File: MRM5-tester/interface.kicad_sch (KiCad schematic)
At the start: 21 parts, among them J1 Conn_01x05, J2 Conn_01x02, J3 GSB1C41110SSHR, J5 Conn_01x02, J6 Conn_01x02, J7 Conn_01x02, U3 CP2102N-A02-GQFN20

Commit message: tester PCB 작성중
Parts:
- removed J5, J6: Conn_01x02, Connector_PinHeader_2.54mm:PinHeader_1x02_P2.54mm_Vertical, symbol PCM_4ms_Connector:Conn_01x02
- added P1, P2: ~, Mouser:PAD_Hole_D2mm, symbol Mouser:PAD_hole2.6
- renumbered C5 to C3, C6 to C4, C7 to C5, C8 to C6, D1 to D5, D2 to D6, D3 to D7, D4 to D8, J3 to J2, J7 to J3, J2 to J4, R3 to R10, R4 to R11, R5 to R12, R6 to R13, R7 to R14, R2 to R9, U3 to U1
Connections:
- new net Vn_h: P2.1
- new net Vp_h: P1.1
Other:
- moved on the sheet: C3, C4, C5, C6, D5, D6, D7, D8, J1, J2, J3, J4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

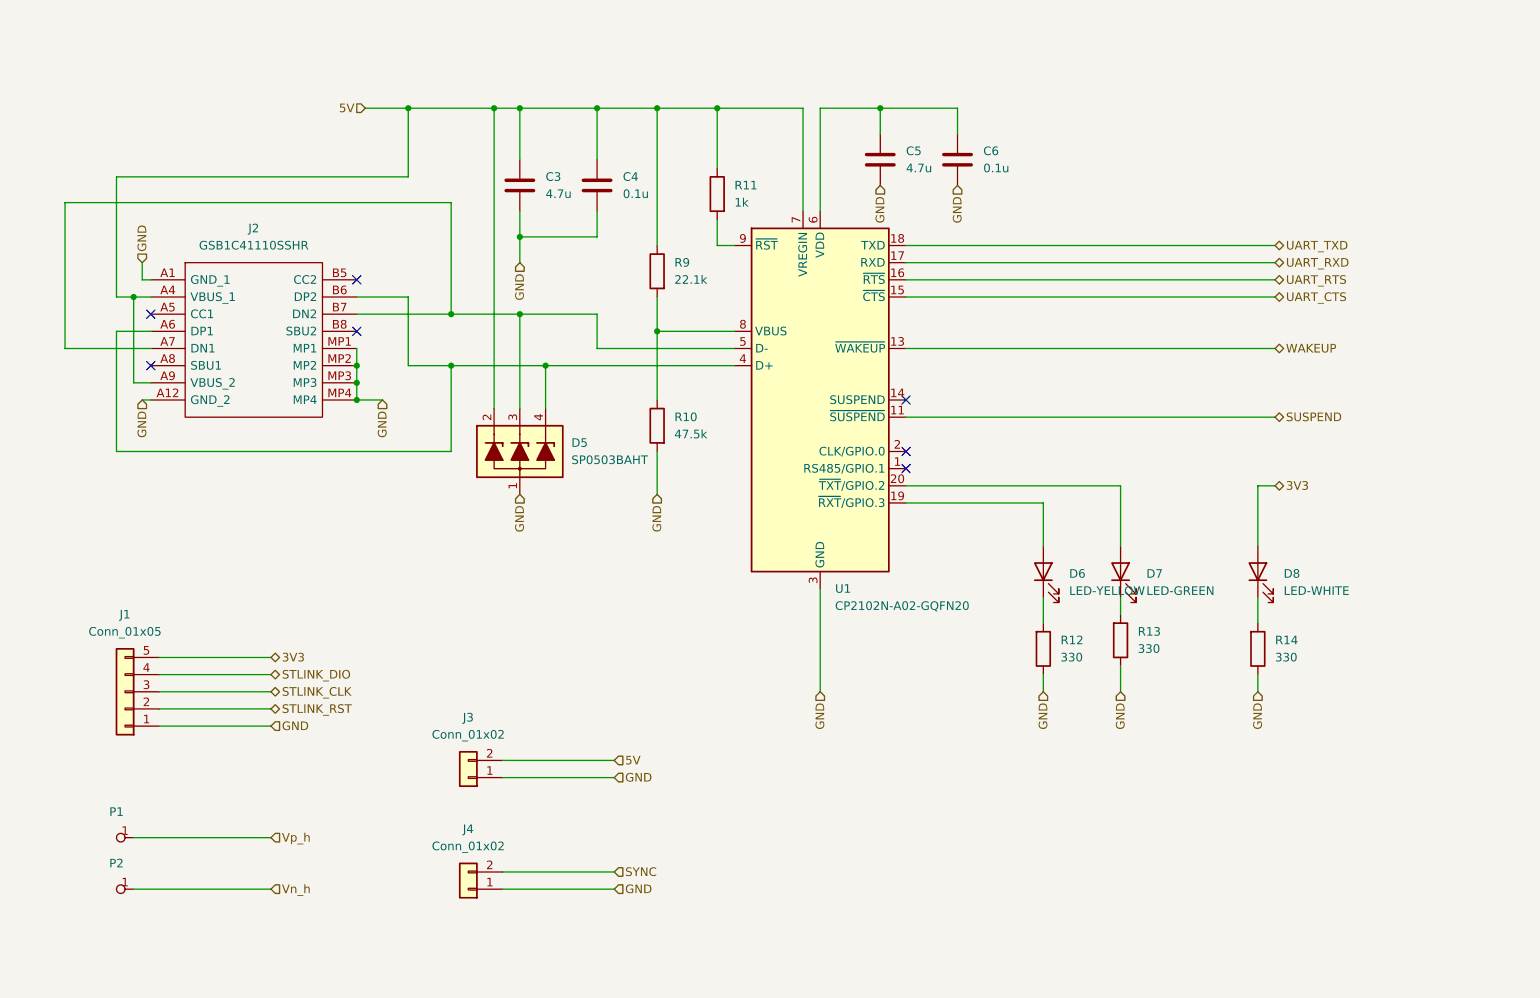
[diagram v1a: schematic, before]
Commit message: tester pcb 디자인 완료
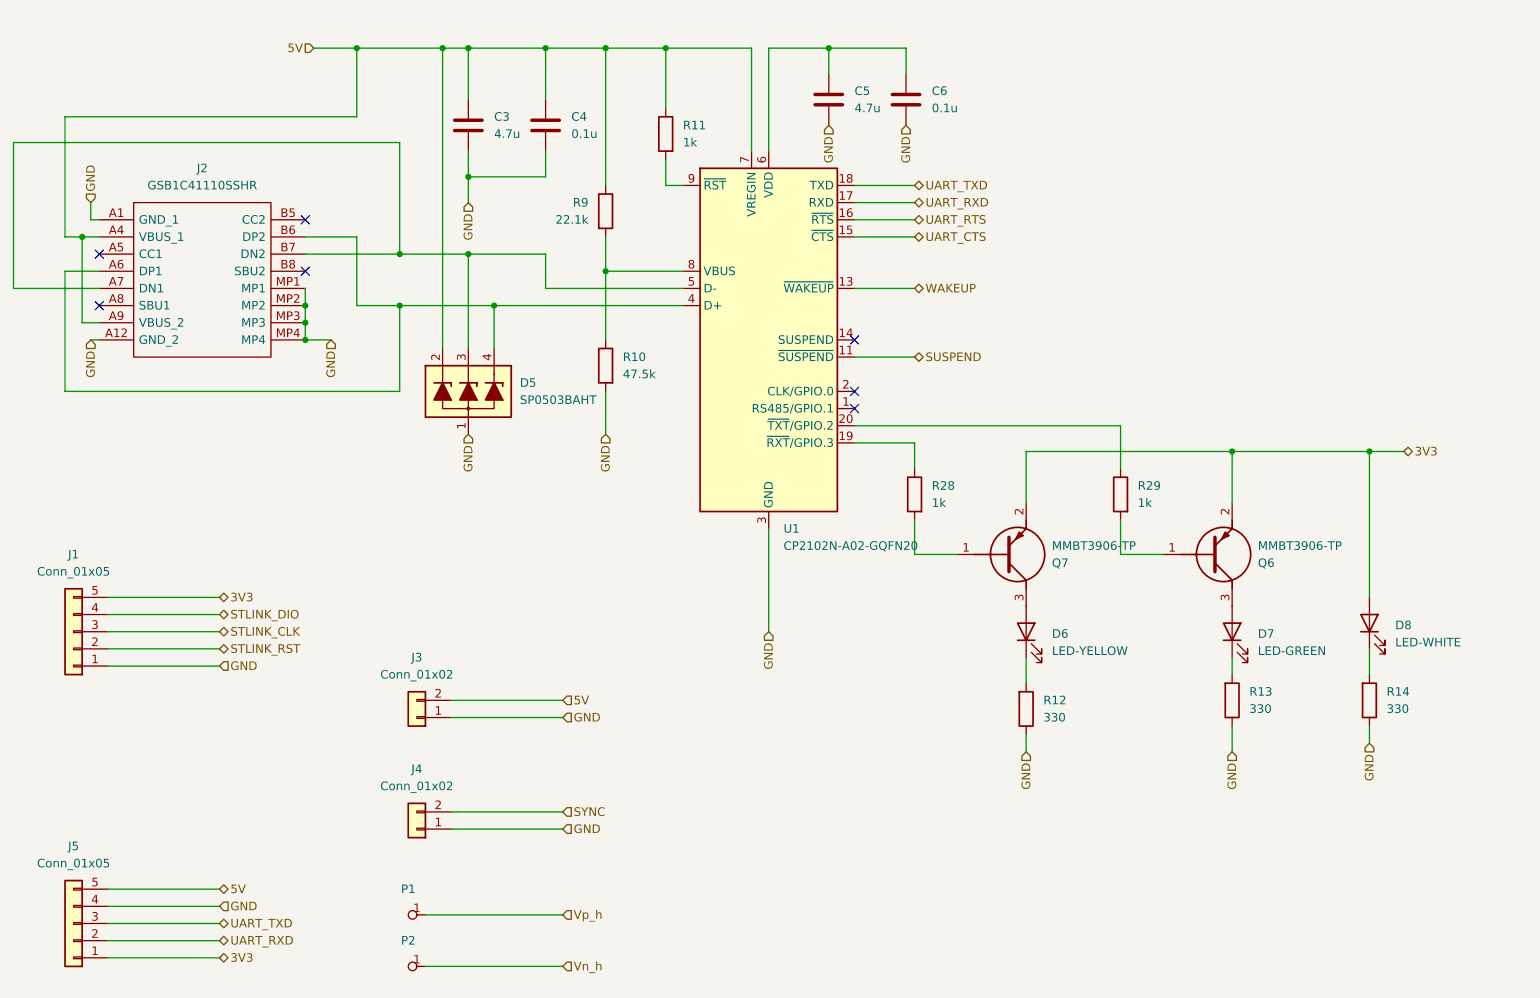
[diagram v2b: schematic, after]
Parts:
- added J5: Conn_01x05, Connector_PinSocket_2.54mm:PinSocket_1x05_P2.54mm_Vertical, symbol Connector_Generic:Conn_01x05
- added Q6, Q7: MMBT3906-TP, Mouser:SOT95P237X125-3N, symbol ktw07182:MMBT3906-TP
- added R28, R29: 1k, PCM_Resistor_SMD_AKL:R_0402_1005Metric, symbol PCM_Resistor_AKL:R_0402
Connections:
- net 3V3: now also J5.1 (Pin_1), Q6.2 (E), Q7.2 (E)
- net 5V: now also J5.5 (Pin_5)
- net GND: now also J5.4 (Pin_4)
- net UART_RXD: now also J5.2 (Pin_2)
- net UART_TXD: now also J5.3 (Pin_3)
- net at U1.19 (~{RXT}/GPIO.3): now also R28.2; no longer D6.2 (A)
- net at U1.20 (~{TXT}/GPIO.2): now also R29.2; no longer D7.2 (A)
- new net: Q7.1 (B), R28.1
- new net: D6.2 (A), Q7.3 (C)
- new net: D7.2 (A), Q6.3 (C)
- new net: Q6.1 (B), R29.1
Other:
- moved on the sheet: C3, C4, C5, C6, D5, D6, D7, D8, J1, J2, J3, J4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

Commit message: tester PCB 검토
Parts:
- added J6: Conn_01x02, Connector_PinHeader_2.54mm:PinHeader_1x02_P2.54mm_Vertical, symbol PCM_4ms_Connector:Conn_01x02
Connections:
- net STLINK_RST: now also J6.2 (Pin_2)
- net WAKEUP: no longer names the net of U1.13 (~{WAKEUP})
- new net PUSH_BTN: J6.1 (Pin_1)
- no-connect marks 7 -> 8
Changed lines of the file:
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@@
+	)
+	(no_connect
+		(at 165.1 76.2)
 	)
 	(no_connect
@@
 	(wire
 		(pts
+			(xy 54.61 148.59) (xy 71.12 148.59)
+		)
+		(stroke
+			(width 0)
+			(type default)
+		)
+	)
+	(wire
+		(pts
 			(xy 220.98 100.33) (xy 220.98 107.95)
 		)
@@
 	(wire
 		(pts
-			(xy 165.1 76.2) (xy 173.99 76.2)
-		)
-		(stroke
-			(width 0)
-			(type default)
-		)
-	)
-	(wire
-		(pts
 			(xy 241.3 100.33) (xy 241.3 121.92)
 		)
@@
 		(pts
 			(xy 119.38 40.64) (xy 128.27 40.64)
+		)
+		(stroke
+			(width 0)
+			(type default)
+		)
+	)
+	(wire
+		(pts
+			(xy 54.61 151.13) (xy 71.12 151.13)
 		)
 		(stroke
@@
 		)
 	)
+	(hierarchical_label "STLINK_RST"
+		(shape bidirectional)
+		(at 71.12 148.59 0)
+		(fields_autoplaced yes)
+		(effects
+			(font
+				(size 1.27 1.27)
+			)
+			(justify left)
+		)
+	)
 	(hierarchical_label "GND"
 		(shape input)
@@
 		)
 	)
-	(hierarchical_label "WAKEUP"
-		(shape bidirectional)
-		(at 173.99 76.2 0)
-		(fields_autoplaced yes)
-		(effects
-			(font
-				(size 1.27 1.27)
-			)
-			(justify left)
-		)
-	)
 	(hierarchical_label "Vn_h"
 		(shape input)
@@
 		(shape input)
 		(at 121.92 153.67 0)
+		(fields_autoplaced yes)
+		(effects
+			(font
+				(size 1.27 1.27)
+			)
+			(justify left)
+		)
+	)
+	(hierarchical_label "PUSH_BTN"
+		(shape bidirectional)
+		(at 71.12 151.13 0)
 		(fields_autoplaced yes)
 		(effects
@@
 					(unit 1)
 				)
+			)
+		)
+	)
+	(symbol
+		(lib_id "PCM_4ms_Connector:Conn_01x02")
+		(at 49.53 151.13 180)
+		(unit 1)
+		(exclude_from_sim no)
+		(in_bom yes)
+		(on_board yes)
+		(dnp no)
+		(fields_autoplaced yes)
+		(property "Reference" "J6"
+			(at 49.53 142.24 0)
+			(effects
+				(font
+					(size 1.27 1.27)
+				)
+			)
+		)
+		(property "Value" "Conn_01x02"
+			(at 49.53 144.78 0)
+			(effects
+				(font
+					(size 1.27 1.27)
+				)
+			)
+		)
+		(property "Footprint" "Connector_PinHeader_2.54mm:PinHeader_1x02_P2.54mm_Vertical"
+			(at 50.165 155.575 0)
+			(effects
+				(font
+					(size 1.27 1.27)
+				)
+				(hide yes)
+			)
+		)
+		(property "Datasheet" ""
+			(at 49.53 151.13 0)
+			(effects
+				(font
+					(size 1.27 1.27)
+				)
+				(hide yes)
+			)
+		)
+		(property "Description" "HEADER 1x2 MALE PINS 0.100” 180deg"
+			(at 49.53 151.13 0)
+			(effects
+				(font
+					(size 1.27 1.27)
+				)
+				(hide yes)
+			)
+		)
+		(property "Specifications" "Pins_01x02, Header, Male Pins, 1*2, spacing 2.54mm, straight pin"
+			(at 52.07 143.256 0)
+			(effects
+				(font
+					(size 1.27 1.27)
+				)
+				(justify left)
+				(hide yes)
+			)
+		)
+		(property "Manufacturer" "TAD"
+			(at 52.07 141.732 0)
+			(effects
+				(font
+					(size 1.27 1.27)
+				)
+				(justify left)
+				(hide yes)
+			)
+		)
+		(property "Part Number" "1-0201FBV0T"
+			(at 52.07 140.208 0)
+			(effects
+				(font
+					(size 1.27 1.27)
+				)
+				(justify left)
+				(hide yes)
+			)
+		)
+		(pin "2"
+		)
+		(pin "1"
+		)
+		(instances
+			(project "MRM5-tester"
+				(path "/6e775c75-0b09-4e5f-9bff-c5585ac94ad7/99281525-64c3-44c6-855e-d443687ecb7a"
+					(reference "J6")
+					(unit 1)
+				)

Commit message: MRM5-tester updated
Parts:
- removed D6: LED-YELLOW, LED_SMD:LED_0402_1005Metric, symbol Device:LED
- removed D7: LED-GREEN, LED_SMD:LED_0402_1005Metric, symbol Device:LED
- removed D8: LED-WHITE, LED_SMD:LED_0402_1005Metric, symbol Device:LED
- added LED5: LED_0603_Red, PCM_LED_SMD_AKL:LED_0603_1608Metric, symbol PCM_LED_AKL:LED_0603_Red
- added LED6: LED_0603_Green, PCM_LED_SMD_AKL:LED_0603_1608Metric, symbol PCM_LED_AKL:LED_0603_Green
- added LED7: LED_0603_White, PCM_LED_SMD_AKL:LED_0603_1608Metric, symbol PCM_LED_AKL:LED_0603_White
- D1: renamed from D5; value SP0503BAHT -> CD143A-SR05; footprint PCM_Package_TO_SOT_SMD_AKL:SOT-143 -> Package_TO_SOT_SMD:SOT-143_Handsoldering
- renumbered J6 to J2, J5 to J3, J2 to J4, J3 to J5, J4 to J6, Q7 to Q5, R28 to R12, R12 to R13, R29 to R14, R13 to R15, R14 to R16
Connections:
- net 3V3: now also LED7.2 (A)
- net 5V: now also D1.4 (L3); no longer D1.2 (L1)
- net at J4.A6 (DP1), J4.B6 (DP2), U1.4 (D+): now also D1.2 (L1); no longer D1.4 (L3)
- net at Q5.3 (C): now also LED5.2 (A)
- net at R15.1: now also LED6.1 (K)
- net at Q6.3 (C): now also LED6.2 (A)
- net at R16.1: now also LED7.1 (K)
- net at R13.1: now also LED5.1 (K)

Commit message: case updated
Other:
- moved on the sheet: J1, J2, J3, J5, J6, P1, P2

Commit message: tester pcb updated
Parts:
- removed J5: Conn_01x02, Connector_PinHeader_2.54mm:PinHeader_1x02_P2.54mm_Vertical, symbol PCM_4ms_Connector:Conn_01x02
- removed LED5: LED_0603_Red, PCM_LED_SMD_AKL:LED_0603_1608Metric, symbol PCM_LED_AKL:LED_0603_Red
- removed LED6: LED_0603_Green, PCM_LED_SMD_AKL:LED_0603_1608Metric, symbol PCM_LED_AKL:LED_0603_Green
- removed LED7: LED_0603_White, PCM_LED_SMD_AKL:LED_0603_1608Metric, symbol PCM_LED_AKL:LED_0603_White
- added J4, J5: PINHD_1x2_Female, Connector_PinSocket_2.54mm:PinSocket_1x02_P2.54mm_Vertical, symbol PCM_SL_Pin_Headers:PINHD_1x2_Female
- added LED5, LED6, LED7: LED_5mm, PCM_LED_THT_AKL:LED_D5.0mm, symbol PCM_LED_AKL:LED_5mm
- renumbered J2 to J1, J6 to J2, J4 to J3, J1 to J6, J3 to J7
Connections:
- net 3V3: now also LED7.2 (A)
- net 5V: now also J5.2
- net GND: now also J5.1
- net at Q5.3 (C): now also LED5.2 (A)
- net at R16.1: now also LED7.1 (K)
- net at R15.1: now also LED6.1 (K)
- net at Q6.3 (C): now also LED6.2 (A)
- net at R13.1: now also LED5.1 (K)
- new net V2n: J4.1
- new net V2p: J4.2
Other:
- moved on the sheet: J1, J2

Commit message: case found!
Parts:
- C3, C5: footprint PCM_Capacitor_SMD_AKL:C_0805_2012Metric_Pad1.15x1.40mm -> PCM_Capacitor_SMD_AKL:C_0603_1608Metric
- C4, C6: value 0.1u -> 100n; footprint PCM_Capacitor_SMD_AKL:C_0402_1005Metric -> PCM_Capacitor_SMD_AKL:C_0603_1608Metric
- Q5, Q6: value MMBT3906-TP -> SMMBT3906LT3G
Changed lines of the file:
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@@
 			)
 		)
-		(property "Footprint" "PCM_Capacitor_SMD_AKL:C_0805_2012Metric_Pad1.15x1.40mm"
+		(property "Footprint" "PCM_Capacitor_SMD_AKL:C_0603_1608Metric"
 			(at 106.9848 48.26 0)
 			(effects
@@
 			)
 		)
-		(property "Value" "MMBT3906-TP"
+		(property "Value" "SMMBT3906LT3G"
 			(at 194.31 114.3001 0)
 			(effects
@@
 			)
 		)
-		(property "Value" "MMBT3906-TP"
+		(property "Value" "SMMBT3906LT3G"
 			(at 224.79 114.3001 0)
 			(effects
@@
 			)
 		)
-		(property "Value" "0.1u"
+		(property "Value" "100n"
 			(at 123.19 53.3399 0)
 			(effects
@@
 			)
 		)
-		(property "Footprint" "PCM_Capacitor_SMD_AKL:C_0402_1005Metric"
+		(property "Footprint" "PCM_Capacitor_SMD_AKL:C_0603_1608Metric"
 			(at 118.4148 48.26 0)
 			(effects
@@
 			)
 		)
-		(property "Footprint" "PCM_Capacitor_SMD_AKL:C_0805_2012Metric_Pad1.15x1.40mm"
+		(property "Footprint" "PCM_Capacitor_SMD_AKL:C_0603_1608Metric"
 			(at 160.3248 44.45 0)
 			(effects
@@
 			)
 		)
-		(property "Value" "0.1u"
+		(property "Value" "100n"
 			(at 176.53 49.5299 0)
 			(effects
@@
 			)
 		)
-		(property "Footprint" "PCM_Capacitor_SMD_AKL:C_0402_1005Metric"
+		(property "Footprint" "PCM_Capacitor_SMD_AKL:C_0603_1608Metric"
 			(at 171.7548 44.45 0)
 			(effects

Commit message: 전류 입력시의 경우를 고려한 회로 추가
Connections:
- net 5V: no longer C3.2, C4.2, D1.4 (L3), J3.A4 (VBUS_1), J3.A9 (VBUS_2), R11.2, R9.2, U1.7 (VREGIN)
- new net: C3.2, C4.2, D1.4 (L3), J3.A4 (VBUS_1), J3.A9 (VBUS_2), R11.2, R9.2, U1.7 (VREGIN)
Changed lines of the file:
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@@
-	)
-	(junction
-		(at 91.44 40.64)
-		(diameter 0)
-		(color 0 0 0 0)
 	)
 	(junction
@@
 	)
 	(junction
+		(at 101.6 40.64)
+		(diameter 0)
+		(color 0 0 0 0)
+	)
+	(junction
 		(at 241.3 100.33)
 		(diameter 0)
@@
 	(wire
 		(pts
-			(xy 118.11 82.55) (xy 111.76 82.55)
-		)
-		(stroke
-			(width 0)
-			(type default)
-		)
-	)
-	(wire
-		(pts
-			(xy 85.09 40.64) (xy 91.44 40.64)
-		)
-		(stroke
-			(width 0)
-			(type default)
-		)
-	)
-	(wire
-		(pts
 			(xy 40.64 54.61) (xy 97.79 54.61)
 		)
@@
 	(wire
 		(pts
+			(xy 101.6 40.64) (xy 107.95 40.64)
+		)
+		(stroke
+			(width 0)
+			(type default)
+		)
+	)
+	(wire
+		(pts
 			(xy 172.72 44.45) (xy 172.72 40.64)
 		)
@@
 	(wire
 		(pts
-			(xy 111.76 82.55) (xy 111.76 85.09)
+			(xy 111.76 68.58) (xy 111.76 85.09)
 		)
 		(stroke
@@
 	(wire
 		(pts
+			(xy 101.6 68.58) (xy 101.6 40.64)
+		)
+		(stroke
+			(width 0)
+			(type default)
+		)
+	)
+	(wire
+		(pts
 			(xy 128.27 160.02) (xy 107.95 160.02)
 		)
@@
 	(wire
 		(pts
-			(xy 91.44 40.64) (xy 107.95 40.64)
+			(xy 91.44 40.64) (xy 101.6 40.64)
 		)
 		(stroke
@@
 		(pts
 			(xy 48.26 68.58) (xy 48.26 50.8)
+		)
+		(stroke
+			(width 0)
+			(type default)
+		)
+	)
+	(wire
+		(pts
+			(xy 111.76 68.58) (xy 101.6 68.58)
 		)
 		(stroke
@@
 		)
 	)
-	(hierarchical_label "5V"
-		(shape input)
-		(at 85.09 40.64 180)
-		(fields_autoplaced yes)
-		(effects
-			(font
-				(size 1.27 1.27)
-			)
-			(justify right)
-		)
-	)
 	(hierarchical_label "3V3"
 		(shape bidirectional)
@@
 	(hierarchical_label "GND"
 		(shape input)
-		(at 107.95 63.5 270)
-		(fields_autoplaced yes)
-		(effects
-			(font
-				(size 1.27 1.27)
-			)
-			(justify right)
+		(at 107.95 63.5 0)
+		(fields_autoplaced yes)
+		(effects
+			(font
+				(size 1.27 1.27)
+			)
+			(justify left)
 		)
 	)
@@
 		(fields_autoplaced yes)
 		(effects
-			(font
-				(size 1.27 1.27)
-			)
-			(justify left)
-		)
-	)
-	(hierarchical_label "5V"
-		(shape input)
-		(at 118.11 82.55 0)
-		(fields_autoplaced yes)
-		(effects
